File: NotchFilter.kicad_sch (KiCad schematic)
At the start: 11 parts, among them U112 LT1169CS8-PBF

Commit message: changed capacitor footprint to match in stock components (0603 to 1206)
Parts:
- C205, C206, C207, C208: footprint Capacitor_SMD:C_0603_1608Metric_Pad1.08x0.95mm_HandSolder -> Capacitor_SMD:C_1206_3216Metric
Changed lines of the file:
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@@
       (effects (font (size 1.27 1.27)))
     )
-    (property "Footprint" "Capacitor_SMD:C_0603_1608Metric_Pad1.08x0.95mm_HandSolder" (at 128.27 87.9348 0)
+    (property "Footprint" "Capacitor_SMD:C_1206_3216Metric" (at 128.27 87.9348 0)
       (effects (font (size 1.27 1.27)) hide)
     )
@@
       (effects (font (size 1.27 1.27)))
     )
-    (property "Footprint" "Capacitor_SMD:C_0603_1608Metric_Pad1.08x0.95mm_HandSolder" (at 162.56 87.9348 0)
+    (property "Footprint" "Capacitor_SMD:C_1206_3216Metric" (at 162.56 87.9348 0)
       (effects (font (size 1.27 1.27)) hide)
     )
@@
       (effects (font (size 1.27 1.27)) (justify left))
     )
-    (property "Footprint" "Capacitor_SMD:C_0603_1608Metric_Pad1.08x0.95mm_HandSolder" (at 136.8552 71.12 0)
+    (property "Footprint" "Capacitor_SMD:C_1206_3216Metric" (at 136.8552 71.12 0)
       (effects (font (size 1.27 1.27)) hide)
     )
@@
       (effects (font (size 1.27 1.27)) (justify left))
     )
-    (property "Footprint" "Capacitor_SMD:C_0603_1608Metric_Pad1.08x0.95mm_HandSolder" (at 148.2852 71.12 0)
-      (effects (font (size 1.27 1.27)) hide)
-    )
+    (property "Footprint" "Capacitor_SMD:C_1206_3216Metric" (at 148.2852 71.12 0)
+      (effects (font (size 1.27 1.27)) hide)
+    )

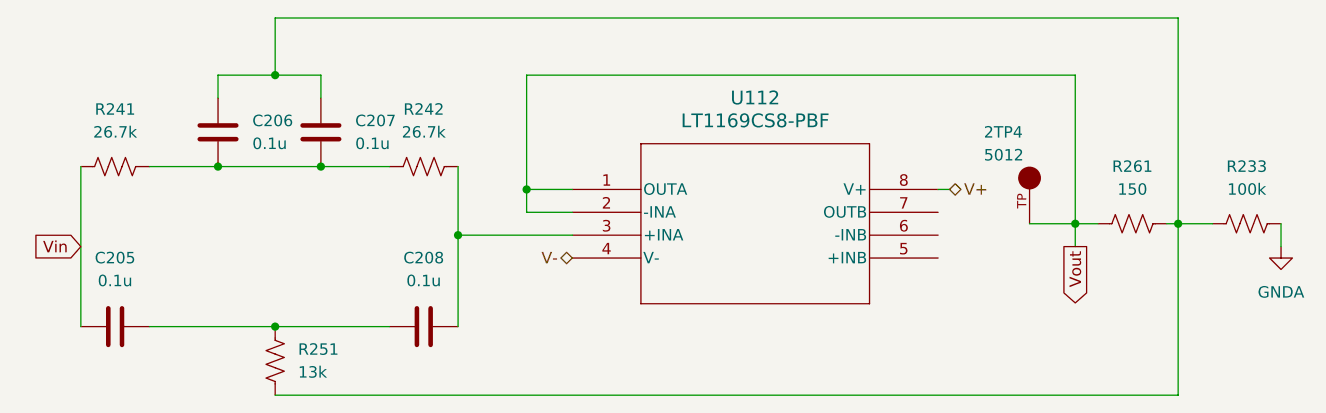
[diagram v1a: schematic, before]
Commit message: first chunk of pcb layout and schematics mods (no connects on pins and changing global labels to hieracarchical labels), one filtering pcb circuit layed out
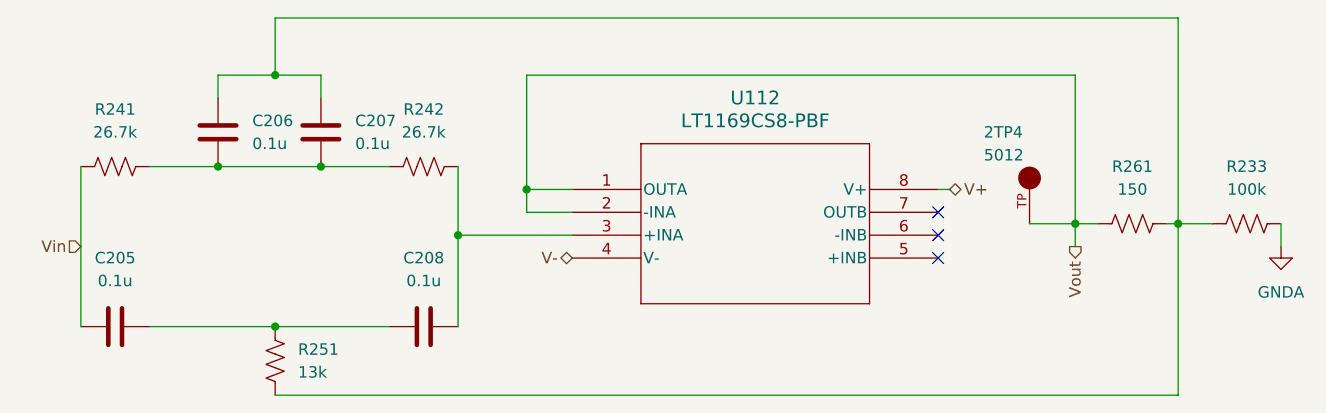
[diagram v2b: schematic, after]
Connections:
- no-connect marks 0 -> 3
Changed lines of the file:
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@@
   (junction (at 170.18 73.66) (diameter 0) (color 0 0 0 0)
   )
+  (no_connect (at 215.9 76.2))
+  (no_connect (at 215.9 81.28))
+  (no_connect (at 215.9 78.74))
   (wire (pts (xy 162.56 78.74) (xy 175.26 78.74))
     (stroke (width 0) (type default))
@@
     (stroke (width 0) (type default))
   )
-  (global_label "Vout" (shape output) (at 231.14 80.01 270) (fields_autoplaced)
-    (effects (font (size 1.27 1.27)) (justify right))
-    (property "Intersheetrefs" "${INTERSHEET_REFS}" (at 231.14 87.1075 90)
-      (effects (font (size 1.27 1.27)) (justify right) hide)
-    )
-  )
-  (global_label "Vin" (shape input) (at 120.65 80.01 180) (fields_autoplaced)
-    (effects (font (size 1.27 1.27)) (justify right))
-    (property "Intersheetrefs" "${INTERSHEET_REFS}" (at 114.8224 80.01 0)
-      (effects (font (size 1.27 1.27)) (justify right) hide)
-    )
-  )
   (hierarchical_label "V-" (shape bidirectional) (at 175.26 81.28 180) (fields_autoplaced)
     (effects (font (size 1.27 1.27)) (justify right))
@@
     (effects (font (size 1.27 1.27)) (justify left))
   )
+  (hierarchical_label "Vin" (shape input) (at 120.65 80.01 180) (fields_autoplaced)
+    (effects (font (size 1.27 1.27)) (justify right))
+  )
+  (hierarchical_label "Vout" (shape output) (at 231.14 80.01 270) (fields_autoplaced)
+    (effects (font (size 1.27 1.27)) (justify right))
+  )
   (symbol (lib_id "Device:R_US") (at 124.46 71.12 90) (unit 1)

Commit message: ToTheEdge,LCSCNums
Moved the 3.5mm connectors to the edge and edited their footprint courtyard so no errors. Adjusted the planes so that it bordered 3.5mm connector pads well and didn't go to edge cuts. Added LCSC part numbers to the parts that were in stock.
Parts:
- 2TP4: LCSC (none) -> C238122
- C205, C206, C207, C208: LCSC (none) -> C2981728
- R233: LCSC (none) -> C2763778
- R241, R242: LCSC (none) -> C870594
- R251: LCSC (none) -> C855609
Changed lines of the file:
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@@
+      (effects (font (size 1.27 1.27)) hide)
+    )
+    (property "LCSC" "C870594" (at 124.46 71.12 0)
       (effects (font (size 1.27 1.27)) hide)
     )
@@
       (effects (font (size 1.27 1.27)) hide)
     )
+    (property "LCSC" "C870594" (at 158.75 71.12 0)
+      (effects (font (size 1.27 1.27)) hide)
+    )
     (pin "1")
     (pin "2")
@@
     )
     (property "Datasheet" "~" (at 124.46 88.9 0)
+      (effects (font (size 1.27 1.27)) hide)
+    )
+    (property "LCSC" "C2981728" (at 124.46 88.9 0)
       (effects (font (size 1.27 1.27)) hide)
     )
@@
     (property "Datasheet" "LT1169CS8-PBF" (at 175.26 73.66 0)
       (effects (font (size 1.27 1.27) italic) hide)
+    )
+    (property "LCSC" "" (at 175.26 73.66 0)
+      (effects (font (size 1.27 1.27)) hide)
     )
     (pin "4")
@@
       (effects (font (size 1.27 1.27)) (justify bottom) hide)
     )
+    (property "LCSC" "C238122" (at 226.06 72.39 0)
+      (effects (font (size 1.27 1.27)) hide)
+    )
     (pin "TP")
     (instances
@@
       (effects (font (size 1.27 1.27)) hide)
     )
+    (property "LCSC" "C855609" (at 142.24 92.71 0)
+      (effects (font (size 1.27 1.27)) hide)
+    )
     (pin "1")
     (pin "2")
@@
       (effects (font (size 1.27 1.27)) hide)
     )
+    (property "LCSC" "C2763778" (at 250.19 77.47 0)
+      (effects (font (size 1.27 1.27)) hide)
+    )
     (pin "1")
     (pin "2")
@@
     )
     (property "Datasheet" "~" (at 158.75 88.9 0)
+      (effects (font (size 1.27 1.27)) hide)
+    )
+    (property "LCSC" "C2981728" (at 158.75 88.9 0)
       (effects (font (size 1.27 1.27)) hide)
     )
@@
       (effects (font (size 1.27 1.27)) hide)
     )
+    (property "LCSC" "C2981728" (at 135.89 67.31 0)
+      (effects (font (size 1.27 1.27)) hide)
+    )
     (pin "1")
     (pin "2")
@@
     )
     (property "Datasheet" "~" (at 237.49 77.47 0)
+      (effects (font (size 1.27 1.27)) hide)
+    )
+    (property "LCSC" "" (at 237.49 77.47 0)
       (effects (font (size 1.27 1.27)) hide)
     )
@@
       (effects (font (size 1.27 1.27)) hide)
     )
+    (property "LCSC" "C2981728" (at 147.32 67.31 0)
+      (effects (font (size 1.27 1.27)) hide)
+    )
